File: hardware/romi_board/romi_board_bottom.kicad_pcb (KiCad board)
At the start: 2 copper layers, 107 x 70 mm, 42 parts, among them J1 Conn_01x14, J2 Conn_01x14, J3 Conn_02x06_Odd_Even, Q1 Q_PMOS_DGS, Q2 Q_PMOS_DGS, SW1 SW_SPST, SW2 SW_SPST, U1 Teensy4.0

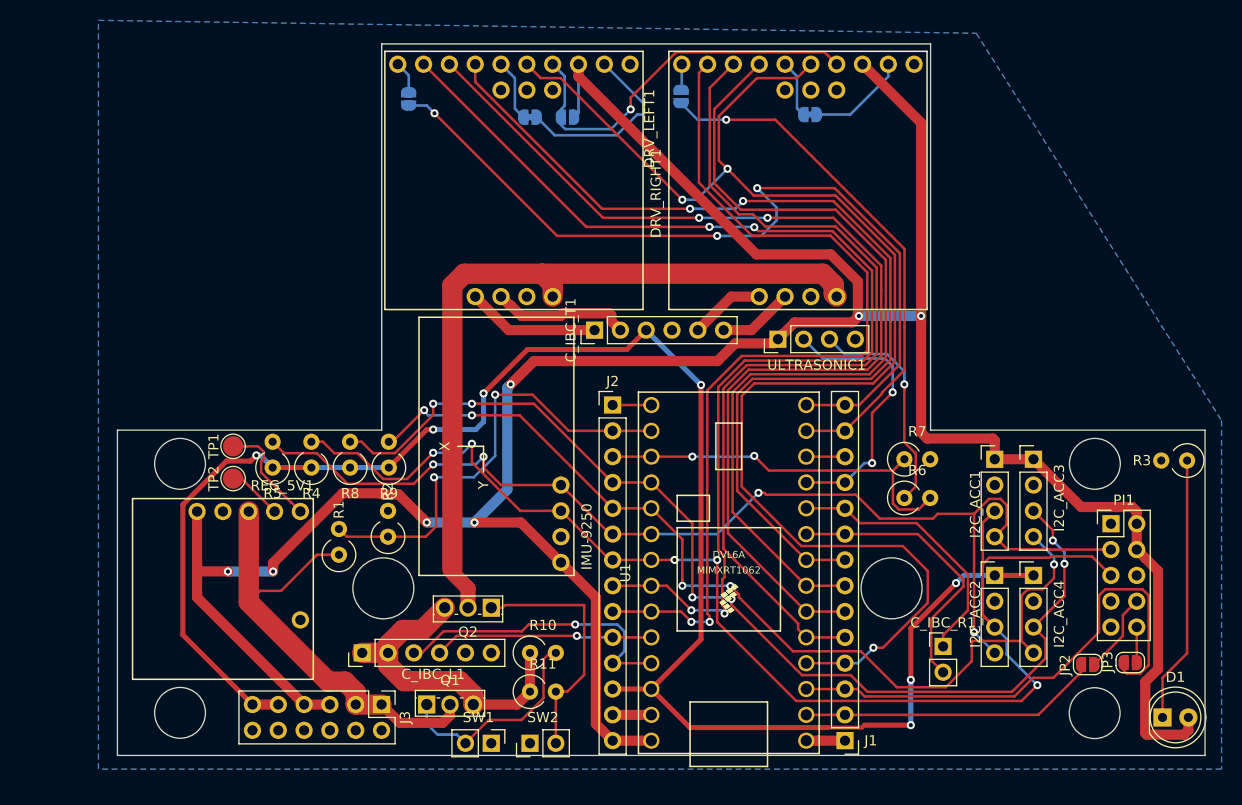
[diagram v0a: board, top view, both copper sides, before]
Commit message: Redesign to use two boards instead of 3
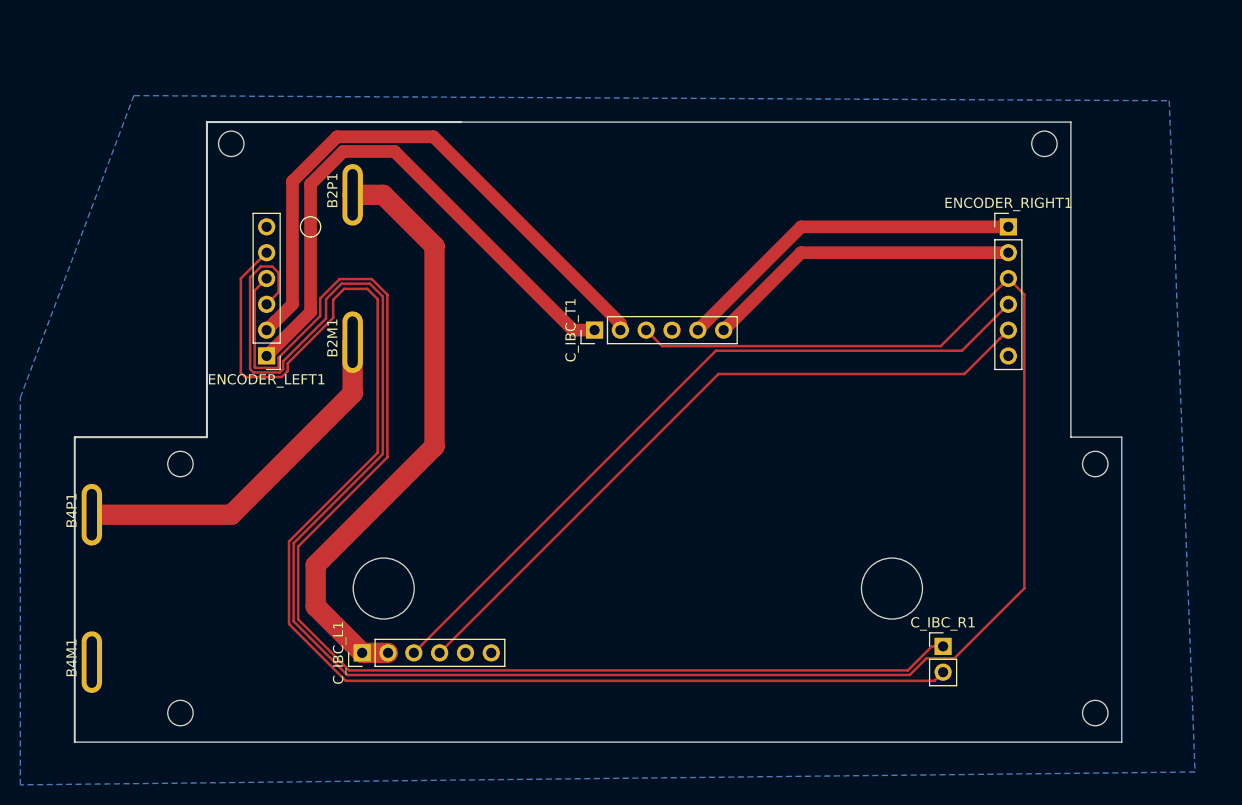
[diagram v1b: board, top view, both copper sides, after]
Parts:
- removed D1: LED, LED_THT:LED_D5.0mm
- removed DRV_LEFT1, DRV_RIGHT1: TB9051FTG, teensy:TB9051FTG_db
- removed I2C_ACC1, I2C_ACC2, I2C_ACC3, I2C_ACC4, ULTRASONIC1: Conn_01x04, Connector_PinHeader_2.54mm:PinHeader_1x04_P2.54mm_Vertical
- removed IMU-9250: Conn_01x04, teensy:MPU9250_BB
- removed J1, J2: Conn_01x14, Connector_PinHeader_2.54mm:PinHeader_1x14_P2.54mm_Vertical
- removed J3: Conn_02x06_Odd_Even, Connector_PinHeader_2.54mm:PinHeader_2x06_P2.54mm_Vertical
- removed JP1, JP2, JP3, JP6, JP7: SolderJumper_2_Open, Jumper:SolderJumper-2_P1.3mm_Open_RoundedPad1.0x1.5mm
- removed JP4, JP5: SolderJumper_2_Bridged, Jumper:SolderJumper-2_P1.3mm_Bridged_RoundedPad1.0x1.5mm
- removed PI1: RASPBERRY_PI_GPIO, Connector_PinHeader_2.54mm:PinHeader_2x05_P2.54mm_Vertical
- removed Q1, Q2: Q_PMOS_DGS, Package_TO_SOT_THT:TO-251-3_Vertical
- removed R1, R10, R11, R2, R3, R4, R5, R8, R9: R_US, Resistor_THT:R_Axial_DIN0309_L9.0mm_D3.2mm_P2.54mm_Vertical
- removed R6, R7: R_Small_US, Resistor_THT:R_Axial_DIN0309_L9.0mm_D3.2mm_P2.54mm_Vertical
- removed REG_5V1: D24V22F5, teensy:D24V2F5_bb
- removed SW1, SW2: SW_SPST, Connector_PinHeader_2.54mm:PinHeader_1x02_P2.54mm_Vertical
- removed TP1, TP2: TestPoint, TestPoint:TestPoint_Pad_D2.0mm
- removed U1: Teensy4.0, teensy:Teensy40_simple
- added B2M1: BTAB, teensy:romi_battery_tab, F.Cu at (73.3, 112.7)
- added B2P1: BTAB, teensy:romi_battery_tab, F.Cu at (73.3, 98.2)
- added B4M1: BTAB, teensy:romi_battery_tab, F.Cu at (47.7, 144.1)
- added B4P1: BTAB, teensy:romi_battery_tab, F.Cu at (47.7, 129.6)
- added ENCODER_LEFT1: Conn_01x06, Connector_PinHeader_2.54mm:PinHeader_1x06_P2.54mm_Vertical, F.Cu at (64.9, 114.0)
- added ENCODER_RIGHT1: Conn_01x06, Connector_PinHeader_2.54mm:PinHeader_1x06_P2.54mm_Vertical, F.Cu at (137.8, 101.3)
- added H1: MountingHole, MountingHole:MountingHole_2.5mm, F.Cu at (61.4, 93.1)
- added H2: MountingHole, MountingHole:MountingHole_2.5mm, F.Cu at (56.4, 124.6)
- added H3: MountingHole, MountingHole:MountingHole_2.5mm, F.Cu at (56.4, 149.1)
- added H4: MountingHole, MountingHole:MountingHole_2.5mm, F.Cu at (146.4, 149.1)
- added H5: MountingHole, MountingHole:MountingHole_2.5mm, F.Cu at (146.4, 124.6)
- added H6: MountingHole, MountingHole:MountingHole_2.5mm, F.Cu at (141.4, 93.1)
- added H7: MountingHole, MountingHole:MountingHole_6mm, F.Cu at (76.4, 136.9)
- added H8: MountingHole, MountingHole:MountingHole_6mm, F.Cu at (126.4, 136.9)
- C_IBC_R1: value Conn_01x04 -> Conn_01x02
- C_IBC_T1: value Conn_01x07 -> Conn_01x06
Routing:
- net +5V: track 288.7 -> 0.00 mm, vias 7 -> 0
- net /XD_EN: track 138.4 -> 0.00 mm, vias 3 -> 0
- net /I2C1_SCL: track 130.4 -> 0.00 mm, vias 5 -> 0
- net /I2C1_SDA: track 112.7 -> 0.00 mm, vias 4 -> 0
- net /LD_OCM: track 112.0 -> 0.00 mm, vias 4 -> 0
- net /I2C2_SCL: track 106.7 -> 0.00 mm, vias 6 -> 0
- net /LENCB: track 28.2 -> 134.6 mm
- net /LD_PWM1: track 104.8 -> 0.00 mm, vias 2 -> 0
- net /LENCA: track 26.7 -> 130.2 mm
- net /LD_PWM2: track 99.8 -> 0.00 mm, vias 2 -> 0
- net /I2C2_SDA: track 95.7 -> 0.00 mm, vias 5 -> 0
- net /RD_OCM: track 90.1 -> 0.00 mm, vias 2 -> 0
- net /RD_PWM1: track 89.3 -> 0.00 mm
- net /RD_PWM2: track 85.5 -> 0.00 mm
- net /TSY_P12: track 84.6 -> 0.00 mm, vias 3 -> 0
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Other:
- board size 107 x 70 mm -> 103 x 61 mm
- net class Med removed
- net class Motor: clearance 0.3 -> 0.2; trace_width 1 -> 1.25
- net class PWR added: clearance 0.6, trace_width 2, via_dia 0.8, via_drill 0.4
- net class Supply removed

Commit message: Added switches, optional USB power connector, changed out mouting holes, a few reroutes for SI
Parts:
- H7, H8: footprint MountingHole:MountingHole_6mm -> teensy:MountingHole_6mm_passthrough
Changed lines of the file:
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@@
       (drillshape 0)
       (scaleselection 1)
-      (outputdirectory "bottom"))
+      (outputdirectory "bottom_board_new"))
   )
   (net 0 "")
@@
     (add_net GND)
   )
+  (module teensy:MountingHole_6mm_passthrough (layer F.Cu)
+    (at 76.392122 136.890976)
+    (descr "Mounting Hole 6mm, no annular")
+    (tags "mounting hole 6mm no annular")
+    (attr virtual)
+    (fp_text reference H7 (at 0 -7) (layer F.SilkS) hide
+      (effects (font (size 1 1) (thickness 0.15)))
+    )
+    (fp_text value MountingHole (at 0 7) (layer F.Fab) hide
+      (effects (font (size 1 1) (thickness 0.15)))
+    )
+    (fp_circle (center 0 0) (end 4 0) (layer F.CrtYd) (width 0.05))
+    (fp_circle (center 0 0) (end 4 0) (layer Cmts.User) (width 0.15))
+    (fp_text user %R (at 0.3 0) (layer F.Fab)
+      (effects (font (size 1 1) (thickness 0.15)))
+    )
+    (pad 1 np_thru_hole circle (at 0 0) (size 6 6) (drill 6) (layers *.Cu *.Mask))
+  )
+  (module teensy:MountingHole_6mm_passthrough (layer F.Cu)
+    (at 126.392122 136.890976)
+    (descr "Mounting Hole 6mm, no annular")
+    (tags "mounting hole 6mm no annular")
+    (attr virtual)
+    (fp_text reference H8 (at 0 -7) (layer F.SilkS) hide
+      (effects (font (size 1 1) (thickness 0.15)))
+    )
+    (fp_text value MountingHole (at 0 7) (layer F.Fab) hide
+      (effects (font (size 1 1) (thickness 0.15)))
+    )
+    (fp_circle (center 0 0) (end 4 0) (layer F.CrtYd) (width 0.05))
+    (fp_circle (center 0 0) (end 4 0) (layer Cmts.User) (width 0.15))
+    (fp_text user %R (at 0.3 0) (layer F.Fab)
+      (effects (font (size 1 1) (thickness 0.15)))
+    )
+    (pad 1 np_thru_hole circle (at 0 0) (size 6 6) (drill 6) (layers *.Cu *.Mask))
+  )
   (module MountingHole:MountingHole_2.5mm (layer F.Cu)
     (at 146.392122 124.640976)
@@
     (pad 1 np_thru_hole circle (at 0 0) (size 2.5 2.5) (drill 2.5) (layers *.Cu *.Mask))
   )
-  (module MountingHole:MountingHole_6mm (layer F.Cu)
-    (at 126.392122 136.890976)
-    (descr "Mounting Hole 6mm, no annular")
-    (tags "mounting hole 6mm no annular")
-    (attr virtual)
-    (fp_text reference H8 (at 0 -7) (layer F.SilkS) hide
-      (effects (font (size 1 1) (thickness 0.15)))
-    )
-    (fp_text value MountingHole (at 0 7) (layer F.Fab) hide
-      (effects (font (size 1 1) (thickness 0.15)))
-    )
-    (fp_text user %R (at 0.3 0) (layer F.Fab)
-      (effects (font (size 1 1) (thickness 0.15)))
-    )
-    (fp_circle (center 0 0) (end 6 0) (layer Cmts.User) (width 0.15))
-    (fp_circle (center 0 0) (end 6.25 0) (layer F.CrtYd) (width 0.05))
-    (pad 1 np_thru_hole circle (at 0 0) (size 6 6) (drill 6) (layers *.Cu *.Mask))
-  )
-  (module MountingHole:MountingHole_6mm (layer F.Cu)
-    (at 76.392122 136.890976)
-    (descr "Mounting Hole 6mm, no annular")
-    (tags "mounting hole 6mm no annular")
-    (attr virtual)
-    (fp_text reference H7 (at 0 -7) (layer F.SilkS) hide
-      (effects (font (size 1 1) (thickness 0.15)))
-    )
-    (fp_text value MountingHole (at 0 7) (layer F.Fab) hide
-      (effects (font (size 1 1) (thickness 0.15)))
-    )
-    (fp_circle (center 0 0) (end 6.25 0) (layer F.CrtYd) (width 0.05))
-    (fp_circle (center 0 0) (end 6 0) (layer Cmts.User) (width 0.15))
-    (fp_text user %R (at 0.3 0) (layer F.Fab)
-      (effects (font (size 1 1) (thickness 0.15)))
-    )
-    (pad 1 np_thru_hole circle (at 0 0) (size 6 6) (drill 6) (layers *.Cu *.Mask))
-  )
   (module MountingHole:MountingHole_2.5mm (layer F.Cu)

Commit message: Fix power/ground terminal swap.
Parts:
- renumbered B2P1 to B2M1, B2M1 to B2P1, B4P1 to B4M1, B4M1 to B4P1
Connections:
- B2M1 pad 1: +BATT -> GND
- B4P1 pad 1: GND -> +BATT
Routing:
- net +BATT: track 59.4 -> 29.5 mm

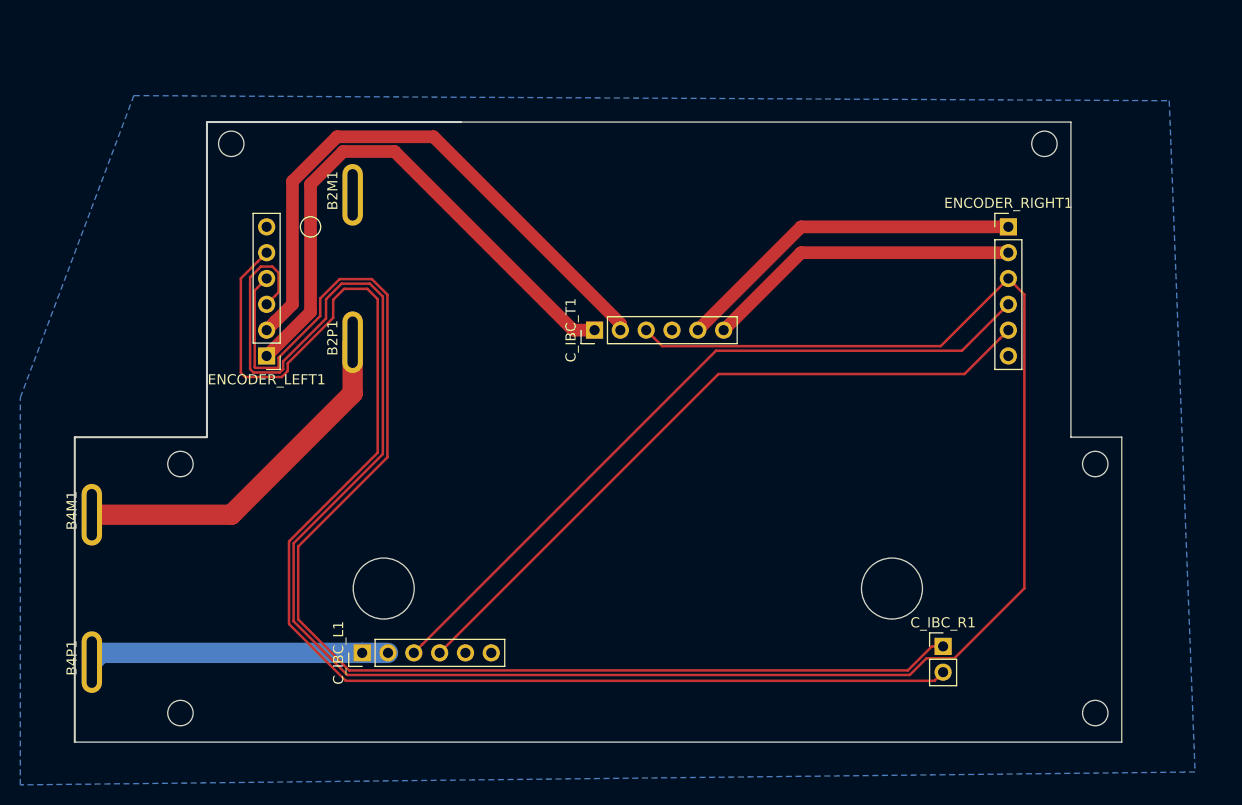
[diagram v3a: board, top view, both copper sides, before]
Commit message: Add power header and filter capacitors to bottom.  Add filter capacitors to top.
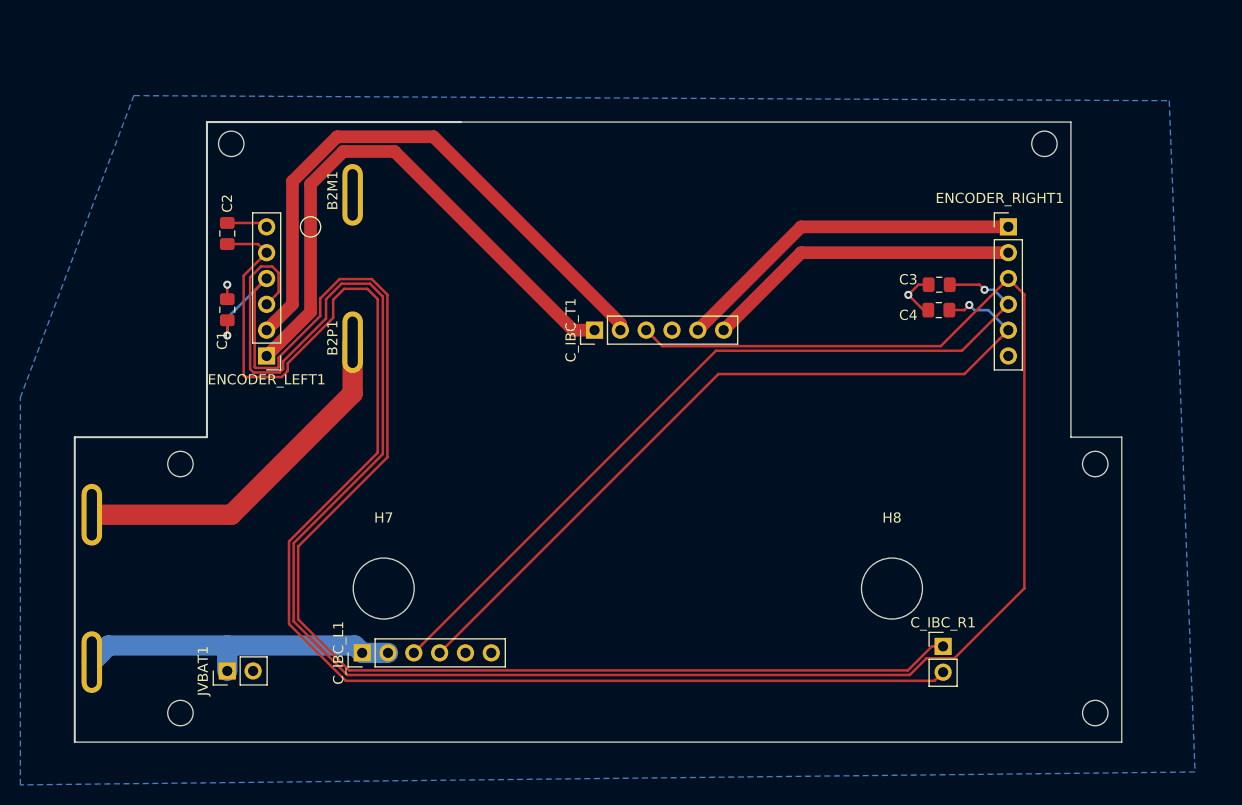
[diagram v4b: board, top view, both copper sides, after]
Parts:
- added C1: 0.1nF, Capacitor_SMD:C_0805_2012Metric_Pad1.18x1.45mm_HandSolder, F.Cu at (61.0, 109.5)
- added C2: 0.1nF, Capacitor_SMD:C_0805_2012Metric_Pad1.18x1.45mm_HandSolder, F.Cu at (61.0, 102.0)
- added C3: 0.1nF, Capacitor_SMD:C_0805_2012Metric_Pad1.18x1.45mm_HandSolder, F.Cu at (131.0, 107.0)
- added C4: 0.1nF, Capacitor_SMD:C_0805_2012Metric_Pad1.18x1.45mm_HandSolder, F.Cu at (131.0, 109.5)
- added JVBAT1: Conn_01x02, Connector_PinHeader_2.54mm:PinHeader_1x02_P2.54mm_Vertical, F.Cu at (61.0, 145.0)
- H7, H8: footprint teensy:MountingHole_6mm_passthrough -> MountingHole:MountingHole_6mm
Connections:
- net +3V3 renamed +3.3V
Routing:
- net GND: track 0.00 -> 10.5 mm, vias 0 -> 2
- net /LENCA: track 130.2 -> 138.9 mm, vias 0 -> 1
- net /RENCB: track 69.1 -> 76.1 mm, vias 0 -> 1
- net /RENCA: track 72.7 -> 79.3 mm, vias 0 -> 1
- net +BATT: track 29.5 -> 33.9 mm
- net /LENCB: track 134.6 -> 138.6 mm
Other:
- net class Default removed
- net class Motor removed
- net class PWR removed
- board text added: "https://github.com/portlandrobotics/common_platform V1.1 2025-08"
